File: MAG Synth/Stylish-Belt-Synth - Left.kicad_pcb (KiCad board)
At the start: 2 copper layers, 88.9 x 101.7 mm, 18 parts, among them J26 WRITE PATCH, J27 PARAM SELECT, J28 PATCH SELECT, J29 MODE, U1 stm32f103c8t6-module-china_smd

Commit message: Latest
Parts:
- removed BT1: 4 x 1.5V, Pin_Headers:Pin_Header_Angled_1x02_Pitch2.54mm
- removed D15: WS2812B, WS2812B
- removed J2: ~, Pin_Headers:Pin_Header_Straight_1x04_Pitch2.54mm
- added CL0: 104, Capacitors_SMD:C_0805_HandSoldering, B.Cu at (142.0, 60.4)
- added CL1: 104, Capacitors_SMD:C_0805_HandSoldering, B.Cu at (158.5, 61.6)
- added CL10: 104, Capacitors_SMD:C_0805_HandSoldering, B.Cu at (129.5, 104.6)
- added CL11: 104, Capacitors_SMD:C_0805_HandSoldering, B.Cu at (123.7, 96.0)
- added CL12: 104, Capacitors_SMD:C_0805_HandSoldering, B.Cu at (121.9, 85.9)
- added CL13: 104, Capacitors_SMD:C_0805_HandSoldering, B.Cu at (123.6, 75.8)
- added CL14: 104, Capacitors_SMD:C_0805_HandSoldering, B.Cu at (129.7, 67.1)
- added CL15: 104, Capacitors_SMD:C_0805_HandSoldering, B.Cu at (138.2, 61.5)
- added CL2: 104, Capacitors_SMD:C_0805_HandSoldering, B.Cu at (167.4, 67.3)
- added CL3: 104, Capacitors_SMD:C_0805_HandSoldering, B.Cu at (173.0, 75.7)
- added CL4: 104, Capacitors_SMD:C_0805_HandSoldering, B.Cu at (175.1, 86.1)
- added CL5: 104, Capacitors_SMD:C_0805_HandSoldering, B.Cu at (172.9, 96.3)
- added CL6: 104, Capacitors_SMD:C_0805_HandSoldering, B.Cu at (167.2, 104.8)
- added CL7: 104, Capacitors_SMD:C_0805_HandSoldering, B.Cu at (158.3, 110.7)
- added CL8: 104, Capacitors_SMD:C_0805_HandSoldering, B.Cu at (148.6, 112.7)
- added CL9: 104, Capacitors_SMD:C_0805_HandSoldering, B.Cu at (138.3, 110.5)
- added D1: 1N4148, SoftEggKiCAD:D_DO-35_SOD27_P7.62mm_Horizontal+SMD, F.Cu at (116.1, 91.7)
- added D2: 1N4148, SoftEggKiCAD:D_DO-35_SOD27_P7.62mm_Horizontal+SMD, F.Cu at (106.0, 105.4)
- added D4: 1N5822, SoftEggKiCAD:D_DO-35_SOD27_P7.62mm_Horizontal+SMD, F.Cu at (119.4, 69.2)
- added J0: USB_B, Connectors:USB_B, B.Cu at (119.8, 62.4)
- added J30: STYLUS, SoftEggKiCAD:LargeRoundTouchPad, B.Cu at (117.5, 147.3)
- added JL1: ~, Pin_Headers:Pin_Header_Straight_1x04_Pitch2.54mm, F.Cu at (152.3, 59.4)
- added REF**: AA Battery Holder, SoftEggKiCAD:AA_Battery_Holder_SoftEgg, B.Cu at (82.9, 104.6)
- added REF**: 1pin, Connect:1pin, F.Cu at (74.2, 60.8)
- added REF**: 1pin, Connect:1pin, F.Cu at (74.2, 149.4)
- added RGB1: WS2812B, WS2812B:WS2812B, F.Cu at (158.8, 61.6)
- added RGB15: WS2812B, WS2812B:WS2812B, F.Cu at (138.2, 61.3)
- added RGB2: WS2812B, WS2812B:WS2812B, F.Cu at (167.3, 67.3)
- added RGB3: WS2812B, WS2812B:WS2812B, F.Cu at (173.0, 75.8)
- added RGB4: WS2812B, WS2812B:WS2812B, F.Cu at (175.0, 86.1)
- added RGB5: WS2812B, WS2812B:WS2812B, F.Cu at (173.0, 96.3)
- added RGB6: WS2812B, WS2812B:WS2812B, F.Cu at (167.3, 104.9)
- added RGB7: WS2812B, WS2812B:WS2812B, F.Cu at (158.6, 110.6)
- KB1: footprint SoftEggKiCAD:MAGWestSynthContactKeybedLeft -> SoftEggKiCAD:MAGWestSynthContactKeybed
- RGB0: renamed from D0; footprint WS2812B -> WS2812B:WS2812B
- RGB10: renamed from D10; footprint WS2812B -> WS2812B:WS2812B
- RGB11: renamed from D11; footprint WS2812B -> WS2812B:WS2812B
- RGB12: renamed from D12; footprint WS2812B -> WS2812B:WS2812B
- RGB13: renamed from D13; footprint WS2812B -> WS2812B:WS2812B
- RGB14: renamed from D14; footprint WS2812B -> WS2812B:WS2812B
- RGB8: renamed from D8; footprint WS2812B -> WS2812B:WS2812B
- RGB9: renamed from D9; footprint WS2812B -> WS2812B:WS2812B
- U1: value stm32f103c8t6-module-china_smd -> stm32f103c8t6-module-china
- moved G*** 3.30 mm to (101.6, 69.8)
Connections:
- J26 pad 1: Net-(J26-Pad1) -> /WRITE
- J27 pad 1: Net-(J27-Pad1) -> /PARAM
- J28 pad 1: Net-(J28-Pad1) -> /PATCH
- KB1 pad 0: Net-(KB1-Pad0) -> /C0
- KB1 pad 1: Net-(KB1-Pad1) -> /C#0
- KB1 pad 10: Net-(KB1-Pad10) -> /A#0
- KB1 pad 11: Net-(KB1-Pad11) -> /B0
- KB1 pad 12: Net-(KB1-Pad12) -> /C1
- KB1 pad 2: Net-(KB1-Pad2) -> /D0
- KB1 pad 3: Net-(KB1-Pad3) -> /D#0
- KB1 pad 4: Net-(KB1-Pad4) -> /E0
- KB1 pad 5: Net-(KB1-Pad5) -> /F0
- KB1 pad 6: Net-(KB1-Pad6) -> /F#0
- KB1 pad 7: Net-(KB1-Pad7) -> /G0
- KB1 pad 8: Net-(KB1-Pad8) -> /G#0
- KB1 pad 9: Net-(KB1-Pad9) -> /A0
- RGB0 pad 1: /WS2812B-16-LED-RING/5V -> /+5V
- RGB0 pad 3: /WS2812B-16-LED-RING/GND -> GND
- RGB0 pad 4: /WS2812B-16-LED-RING/DIN -> /LED_DIN
- RGB10 pad 1: /WS2812B-16-LED-RING/5V -> /+5V
- RGB10 pad 3: /WS2812B-16-LED-RING/GND -> GND
- RGB11 pad 1: /WS2812B-16-LED-RING/5V -> /+5V
- RGB11 pad 3: /WS2812B-16-LED-RING/GND -> GND
- RGB12 pad 1: /WS2812B-16-LED-RING/5V -> /+5V
- RGB12 pad 3: /WS2812B-16-LED-RING/GND -> GND
- RGB13 pad 1: /WS2812B-16-LED-RING/5V -> /+5V
- RGB13 pad 3: /WS2812B-16-LED-RING/GND -> GND
- RGB14 pad 1: /WS2812B-16-LED-RING/5V -> /+5V
- RGB14 pad 3: /WS2812B-16-LED-RING/GND -> GND
- RGB8 pad 1: /WS2812B-16-LED-RING/5V -> /+5V
- RGB8 pad 3: /WS2812B-16-LED-RING/GND -> GND
- RGB9 pad 1: /WS2812B-16-LED-RING/5V -> /+5V
- RGB9 pad 3: /WS2812B-16-LED-RING/GND -> GND
- U1 pad 1: (no net) -> /C0
- U1 pad 10: (no net) -> /A0
- U1 pad 11: (no net) -> /A#0
- U1 pad 2: (no net) -> /C#0
- U1 pad 3: (no net) -> /D0
- U1 pad 30: (no net) -> /C2
- U1 pad 31: (no net) -> /G0
- U1 pad 32: (no net) -> /LED_DIN
- U1 pad 33: (no net) -> /PARAM
- U1 pad 34: (no net) -> /WRITE
- U1 pad 35: (no net) -> /PATCH
- U1 pad 36: (no net) -> /G#0
- U1 pad 37: (no net) -> Net-(U1-Pad37)
- U1 pad 38: (no net) -> Net-(U1-Pad38)
- U1 pad 39: (no net) -> GND
- U1 pad 4: (no net) -> /D#0
- U1 pad 40: (no net) -> GND
- U1 pad 5: (no net) -> /E0
- U1 pad 6: (no net) -> /F0
- U1 pad 7: (no net) -> /F#0
- U1 pad 8: (no net) -> Net-(J0-Pad2)
- U1 pad 9: (no net) -> Net-(J0-Pad3)
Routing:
- net GND: track 0.00 -> 457.8 mm, vias 0 -> 15
- net /WS2812B-16-LED-RING/GND: track 296.0 -> 0.00 mm, vias 8 -> 0
- net /+5V: track 0.00 -> 267.1 mm, vias 0 -> 17
- net /LED_DIN: track 0.00 -> 256.1 mm, vias 0 -> 1
- net /WS2812B-16-LED-RING/DIN: track 228.9 -> 0.00 mm, vias 1 -> 0
- net /G#0: track 0.00 -> 166.6 mm, vias 0 -> 1
- net /WS2812B-16-LED-RING/5V: track 161.7 -> 0.00 mm, vias 7 -> 0
- net /WRITE: track 0.00 -> 151.2 mm, vias 0 -> 1
- net /G0: track 0.00 -> 147.7 mm, vias 0 -> 1
- net /PARAM: track 0.00 -> 142.8 mm, vias 0 -> 1
- net Net-(J27-Pad1): track 136.7 -> 0.00 mm, vias 1 -> 0
- net Net-(D1-Pad1): track 153.1 -> 17.7 mm, vias 1 -> 0
- net Net-(KB1-Pad5): track 124.6 -> 0.00 mm, vias 1 -> 0
- net /PATCH: track 0.00 -> 115.1 mm, vias 0 -> 1
- net Net-(J26-Pad1): track 114.9 -> 0.00 mm, vias 1 -> 0
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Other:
- board size 88.9 x 101.7 mm -> 126.6 x 101.7 mm
- net class Default: trace_width 0.508 -> 0.2
- board text added: "20"
- board text added: "Stylish!"
- board text removed: "+5"
- board text removed: "GND"

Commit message: Moving around the gerbers
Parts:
- removed G***: LOGO, SoftEggKiCAD:SOFTEGG_LOGO2
- removed JL1: ~, Pin_Headers:Pin_Header_Straight_1x04_Pitch2.54mm
- removed REF**: AA Battery Holder, SoftEggKiCAD:AA_Battery_Holder_SoftEgg
- removed REF** (x2): 1pin, Connect:1pin
- added ?: 1pin, Connect:1pin, F.Cu at (79.2, 66.4)
- added BT12: ~, SoftEggKiCAD:AA_Battery_Dual_Terminal, B.Cu at (95.2, 134.2)
- added BTN1: -, SoftEggKiCAD:AA_Battery_-_Terminal, B.Cu at (109.2, 78.1)
- added BTP2: +, SoftEggKiCAD:AA_Battery_+_Terminal, B.Cu at (95.2, 78.1)
- added C1: 1μF, SoftEggKiCAD:C_Disc_D5.0mm_W2.5mm_P5.00mm+SMD, B.Cu at (114.9, 67.0)
- added CA4: 0.39μF, SoftEggKiCAD:C_Disc_D5.0mm_W2.5mm_P5.00mm+SMD, F.Cu at (104.8, 58.3)
- added D3: 1N5822, SoftEggKiCAD:D_DO-35_SOD27_P7.62mm_Horizontal+SMD, F.Cu at (87.6, 72.4)
- added R1: 8Ω, SoftEggKiCAD:R_Axial_DIN0204_L3.6mm_D1.6mm_P7.62mm_Horizontal+SMD804, B.Cu at (111.8, 66.8)
- added R2: 47Ω, SoftEggKiCAD:R_Axial_DIN0204_L3.6mm_D1.6mm_P7.62mm_Horizontal+SMD804, B.Cu at (100.6, 66.5)
- added R3: 120Ω, SoftEggKiCAD:R_Axial_DIN0204_L3.6mm_D1.6mm_P7.62mm_Horizontal+SMD804, F.Cu at (125.2, 108.1)
- added RA1: 100Ω, SoftEggKiCAD:R_Axial_DIN0204_L3.6mm_D1.6mm_P7.62mm_Horizontal+SMD804, F.Cu at (108.0, 64.1)
- added RV1: Volume, SoftEggKiCAD:Wheel_Pot_W_Switch_RV12_B103_FUSTAR, B.Cu at (94.2, 59.4)
- added SW1: OVERDRIVE, Pin_Headers:Pin_Header_Straight_1x03_Pitch2.54mm, B.Cu at (108.6, 70.5)
- KB1: footprint SoftEggKiCAD:MAGWestSynthContactKeybed -> SoftEggKiCAD:MAGWestSynthContactKeybedLeft2
- moved D4 31.8 mm to (87.6, 70.0), turned to 0 degrees
- moved D1 16.1 mm to (102.4, 83.1), turned to 180 degrees
- moved CL0 6.46 mm to (148.5, 60.2), turned to 45 degrees
- moved J30 2.69 mm to (118.4, 144.8)
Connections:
- CL0 pad 1: /+5V -> /VIN
- CL1 pad 1: /+5V -> /VIN
- CL10 pad 1: /+5V -> /VIN
- CL11 pad 1: /+5V -> /VIN
- CL12 pad 1: /+5V -> /VIN
- CL13 pad 1: /+5V -> /VIN
- CL14 pad 1: /+5V -> /VIN
- CL15 pad 1: /+5V -> /VIN
- CL2 pad 1: /+5V -> /VIN
- CL3 pad 1: /+5V -> /VIN
- CL4 pad 1: /+5V -> /VIN
- CL5 pad 1: /+5V -> /VIN
- CL6 pad 1: /+5V -> /VIN
- CL7 pad 1: /+5V -> /VIN
- CL8 pad 1: /+5V -> /VIN
- CL9 pad 1: /+5V -> /VIN
- D4 pad 1: /+5V -> /VUSB
- RGB0 pad 1: /+5V -> /VIN
- RGB1 pad 1: /+5V -> /VIN
- RGB10 pad 1: /+5V -> /VIN
- RGB11 pad 1: /+5V -> /VIN
- RGB12 pad 1: /+5V -> /VIN
- RGB13 pad 1: /+5V -> /VIN
- RGB14 pad 1: /+5V -> /VIN
- RGB15 pad 1: /+5V -> /VIN
- RGB15 pad 2: /WS2812B-16-LED-RING/DOUT -> /DOUT
- RGB2 pad 1: /+5V -> /VIN
- RGB3 pad 1: /+5V -> /VIN
- RGB4 pad 1: /+5V -> /VIN
- RGB5 pad 1: /+5V -> /VIN
- RGB6 pad 1: /+5V -> /VIN
- RGB7 pad 1: /+5V -> /VIN
- RGB8 pad 1: /+5V -> /VIN
- RGB9 pad 1: /+5V -> /VIN
- U1 pad 38: Net-(U1-Pad38) -> /+3.3V
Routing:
- net /VIN: track 0.00 -> 248.2 mm, vias 0 -> 16
- net /LED_DIN: track 256.1 -> 60.2 mm, vias 1 -> 0
- net Net-(BTP4-Pad1): track 0.00 -> 184.3 mm
- net /+5V: track 267.1 -> 89.0 mm, vias 17 -> 1
- net /+3.3V: track 0.00 -> 166.0 mm, vias 0 -> 1
- net /AUDIO_OUT: track 45.3 -> 183.9 mm, vias 0 -> 2
- net GND: track 457.8 -> 536.8 mm, vias 15 -> 18
- net /F0: track 111.6 -> 47.4 mm
- net Net-(RA1-Pad1): track 0.00 -> 62.8 mm
- net /B1: track 47.9 -> 0.00 mm
- net /A1: track 74.4 -> 29.4 mm
- net /F1: track 51.3 -> 14.2 mm, vias 1 -> 0
- net /G#1: track 62.6 -> 25.9 mm
- net /A#1: track 61.3 -> 26.8 mm
- net /C2: track 66.6 -> 32.6 mm
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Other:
- board size 126.6 x 101.7 mm -> 121.1 x 101.7 mm
- net class Default: trace_width 0.2 -> 0.635; via_dia 2.032 -> 1.524
- board text added: "+"
- board text added: "+5V"
- board text added: "-"
- board text added: "3.3V"
- board text added: "AUD"
- board text added: "GND"
- board text added: "L"
- board text removed: "MODE"
- board text removed: "PATCH"
- board text removed: "Stylish!"
- board text removed: "VALUE"
- board text removed: "WRITE"

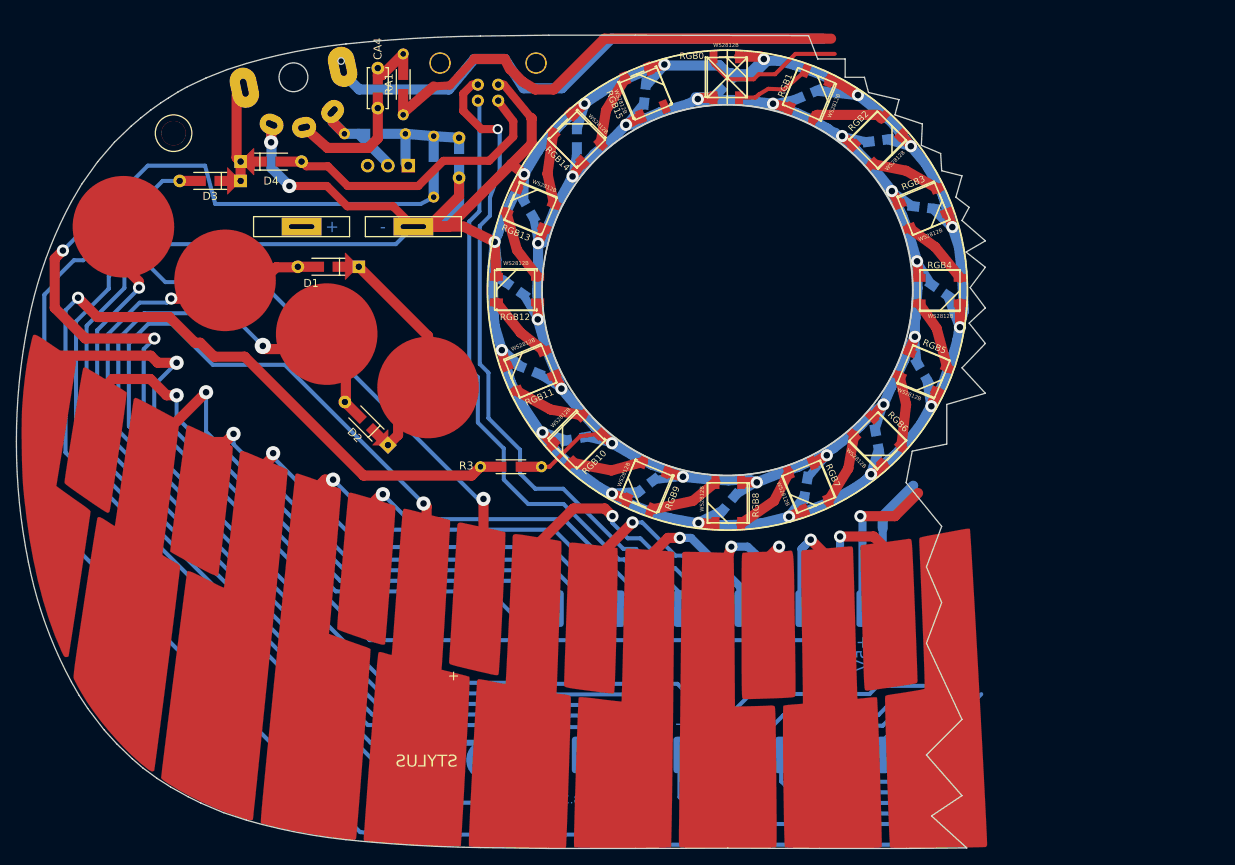
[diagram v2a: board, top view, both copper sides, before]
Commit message: PCB V4 update Wood CNC models added
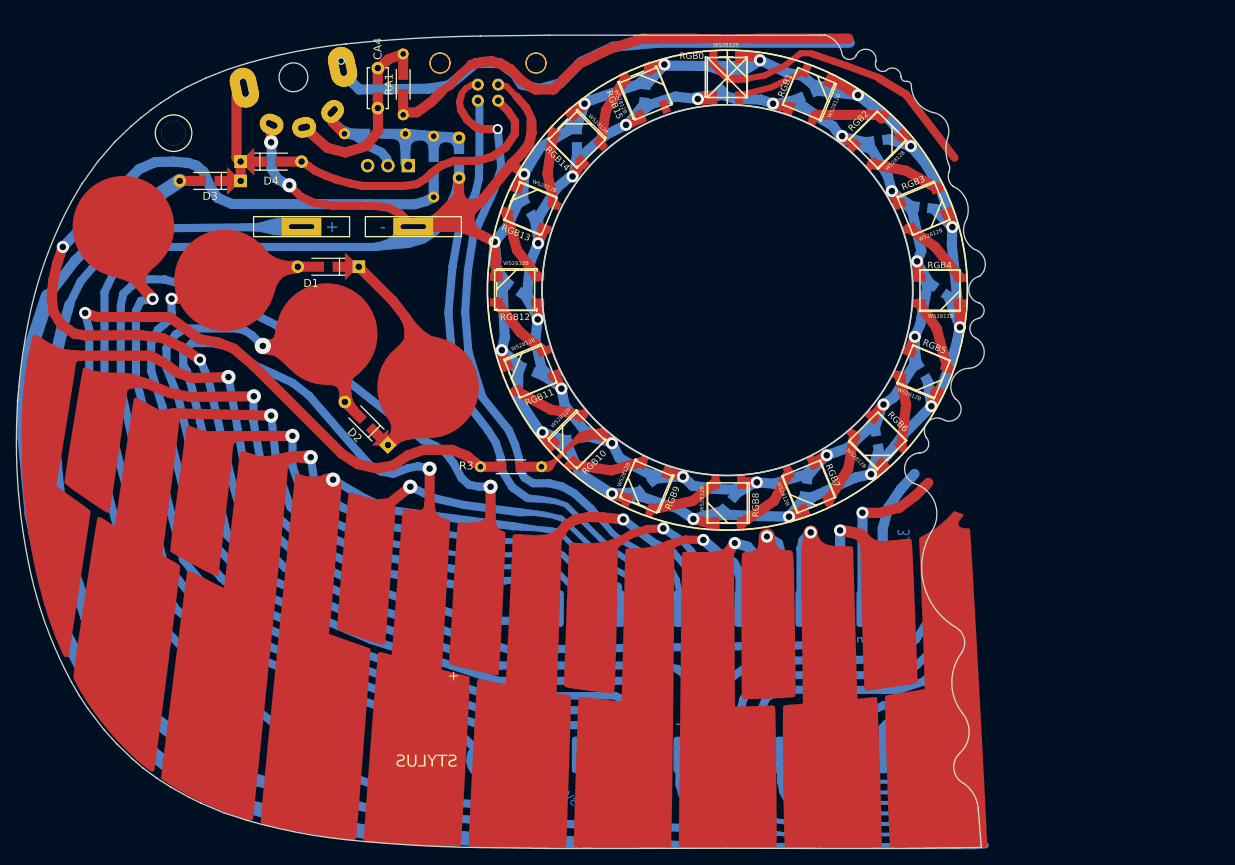
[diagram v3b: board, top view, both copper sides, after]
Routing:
- net Net-(BTN3-Pad1): track 0.00 -> 193.5 mm
- net /B1: track 0.00 -> 36.8 mm
- net /LED_DIN: track 60.2 -> 80.8 mm
- net /PARAM: track 135.5 -> 122.5 mm
- net /G0: track 150.3 -> 138.7 mm
- net /VIN: track 248.2 -> 258.4 mm
- net /C2: track 32.6 -> 41.5 mm
- net /A#1: track 26.8 -> 35.5 mm
- net GND: track 536.8 -> 544.6 mm
- net /G#0: track 164.3 -> 157.4 mm
- net Net-(BTP4-Pad1): track 184.3 -> 190.9 mm
- net /+3.3V: track 166.0 -> 161.6 mm
- net /F1: track 14.2 -> 18.2 mm
- net /PATCH: track 111.5 -> 107.8 mm
- net /C#0: track 70.9 -> 74.4 mm
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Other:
- outline, holes or cut-outs redrawn
- board text added: "5"
- board text added: "G"
- board text removed: "+5V"
